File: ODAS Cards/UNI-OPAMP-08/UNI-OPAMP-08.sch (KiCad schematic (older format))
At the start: 66 parts, among them U1 LM324N, U2 LM324N

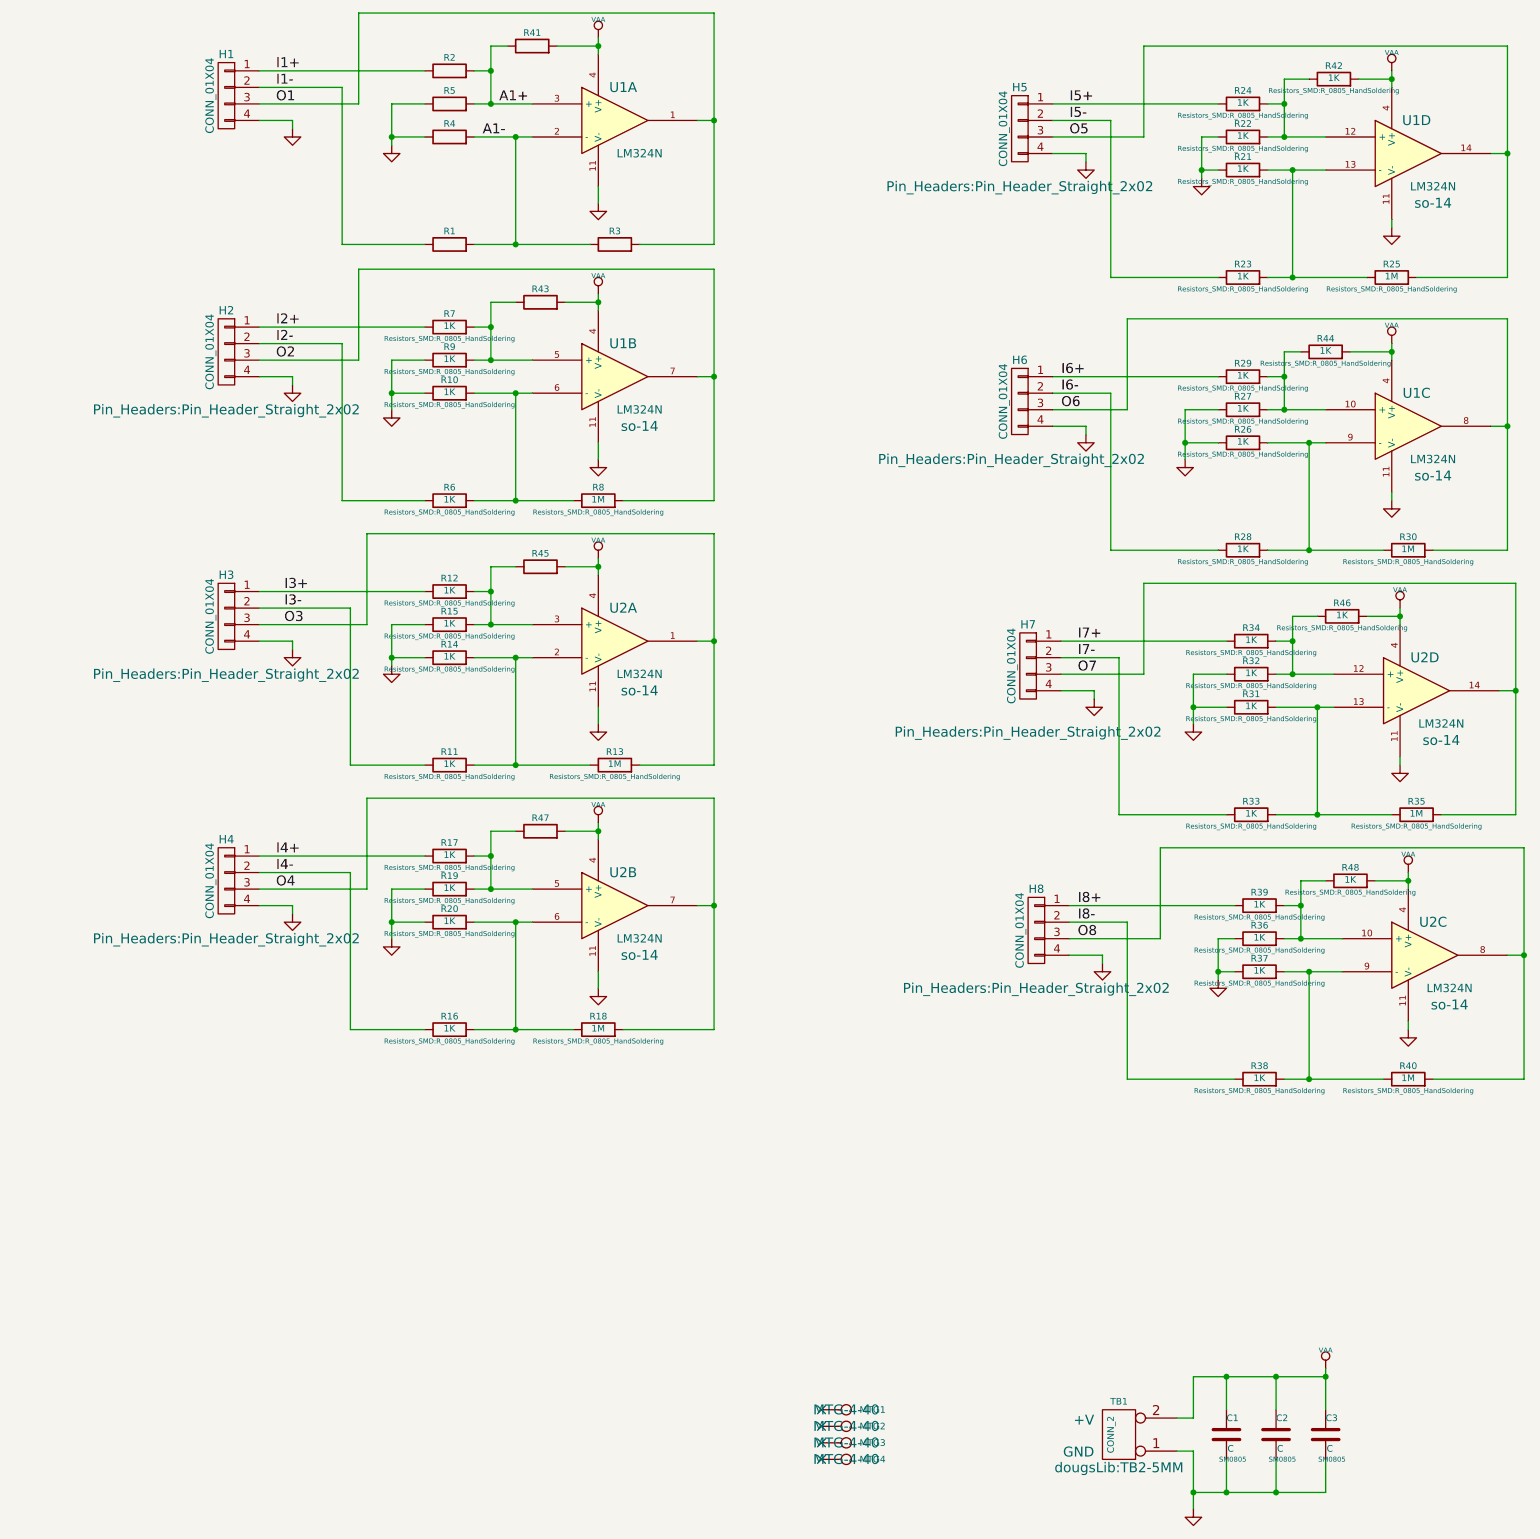
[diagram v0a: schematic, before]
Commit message: Added sixth resistor splitting pwr/gnd to A+ input
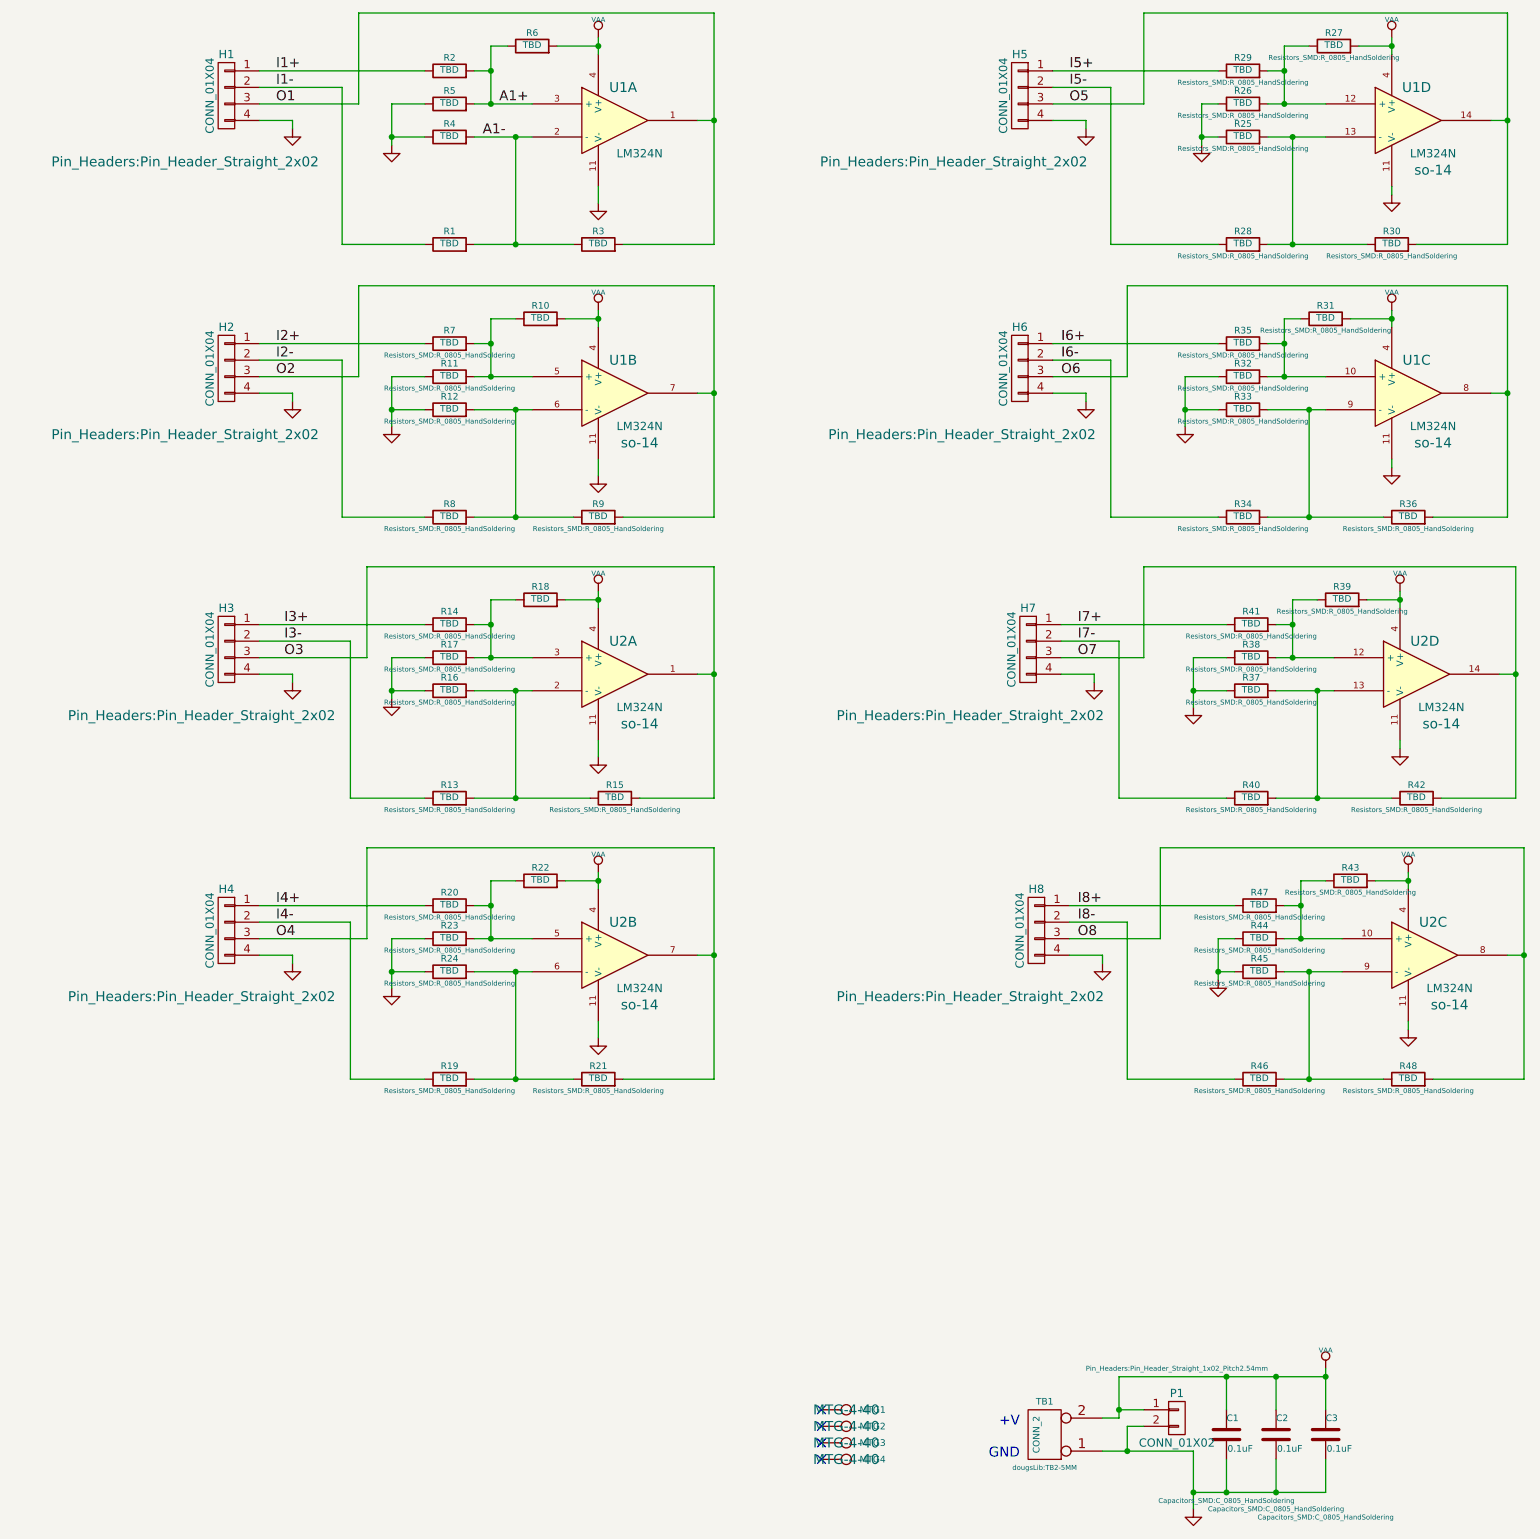
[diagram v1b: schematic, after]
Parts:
- added P1: CONN_01X02, Pin_Headers:Pin_Header_Straight_1x02_Pitch2.54mm, symbol CONN_01X02
- C1, C2, C3: value C -> 0.1uF; footprint SM0805 -> Capacitors_SMD:C_0805_HandSoldering
- R1, R2, R4, R5, R7: value 1K -> TBD
- R10: renamed from R43; value 1K -> TBD
- R11: renamed from R9; value 1K -> TBD
- R12: renamed from R10; value 1K -> TBD
- R13: renamed from R11; value 1K -> TBD
- R14: renamed from R12; value 1K -> TBD
- R15: renamed from R13; value 1M -> TBD
- R16: renamed from R14; value 1K -> TBD
- R17: renamed from R15; value 1K -> TBD
- R18: renamed from R45; value 1K -> TBD
- R19: renamed from R16; value 1K -> TBD
- R20: renamed from R17; value 1K -> TBD
- R21: renamed from R18; value 1M -> TBD
- R22: renamed from R47; value 1K -> TBD
- R23: renamed from R19; value 1K -> TBD
- R24: renamed from R20; value 1K -> TBD
- R25: renamed from R21; value 1K -> TBD
- R26: renamed from R22; value 1K -> TBD
- R27: renamed from R42; value 1K -> TBD
- R28: renamed from R23; value 1K -> TBD
- R29: renamed from R24; value 1K -> TBD
- R3: value 1M -> TBD
- R30: renamed from R25; value 1M -> TBD
- R31: renamed from R44; value 1K -> TBD
- R32: renamed from R27; value 1K -> TBD
- R33: renamed from R26; value 1K -> TBD
- R34: renamed from R28; value 1K -> TBD
- R35: renamed from R29; value 1K -> TBD
- R36: renamed from R30; value 1M -> TBD
- R37: renamed from R31; value 1K -> TBD
- R38: renamed from R32; value 1K -> TBD
- R39: renamed from R46; value 1K -> TBD
- R40: renamed from R33; value 1K -> TBD
- R41: renamed from R34; value 1K -> TBD
- R42: renamed from R35; value 1M -> TBD
- R43: renamed from R48; value 1K -> TBD
- R44: renamed from R36; value 1K -> TBD
- R45: renamed from R37; value 1K -> TBD
- R46: renamed from R38; value 1K -> TBD
- R47: renamed from R39; value 1K -> TBD
- R48: renamed from R40; value 1M -> TBD
- R6: renamed from R41; value 1K -> TBD
- R8: renamed from R6; value 1K -> TBD
- R9: renamed from R8; value 1M -> TBD
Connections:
- net GND: now also P1.2 (P2)
- net VAA: now also P1.1 (P1)
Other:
- moved on the sheet: H2, H3, H4, H5, H6, H7, R10, R11, R12, R13, R14, R15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
